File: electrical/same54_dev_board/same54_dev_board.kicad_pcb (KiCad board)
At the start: 2 copper layers, 177.8 x 83.8 mm, 0 parts

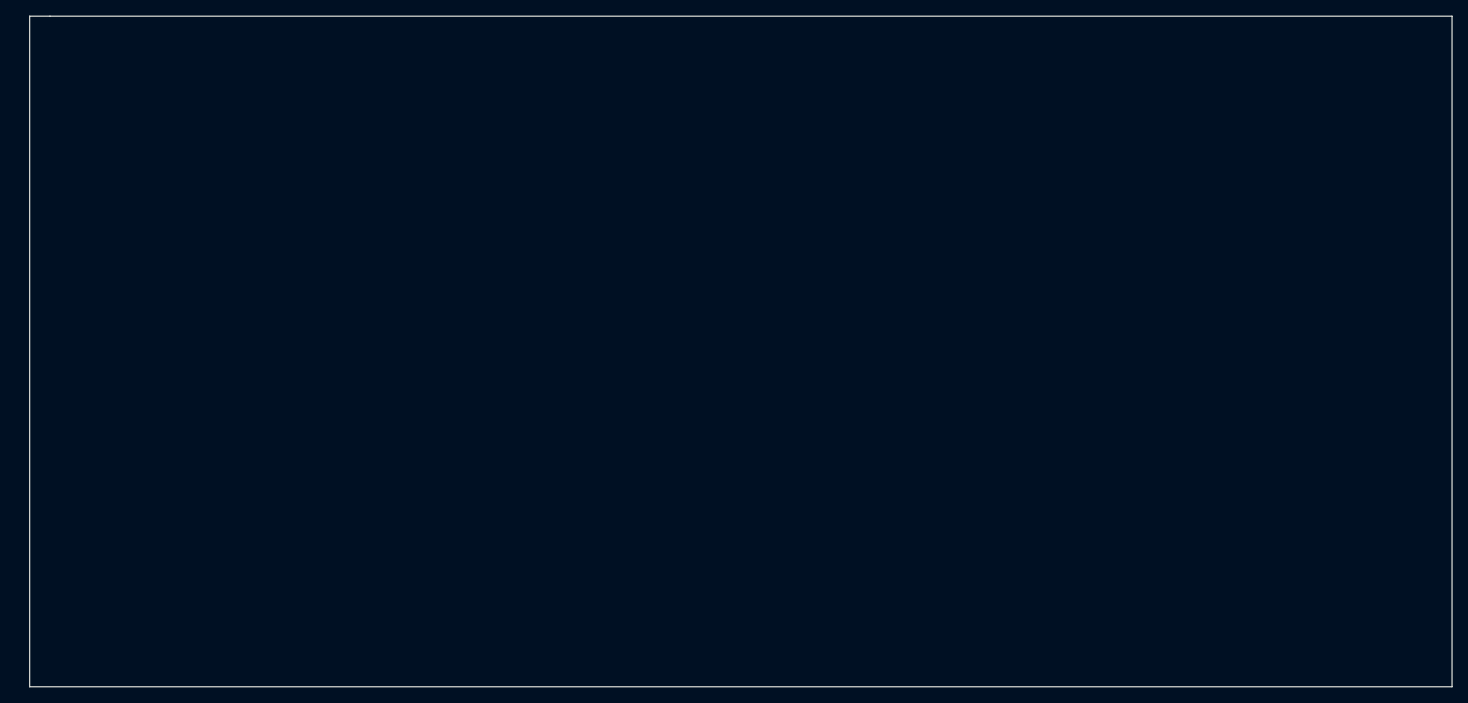
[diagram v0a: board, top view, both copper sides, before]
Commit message: Added hierarchical pins for some components, finished io expander to lcd bus, going with 2x20 icd block header for the tft bus but dont have a part number for digikey
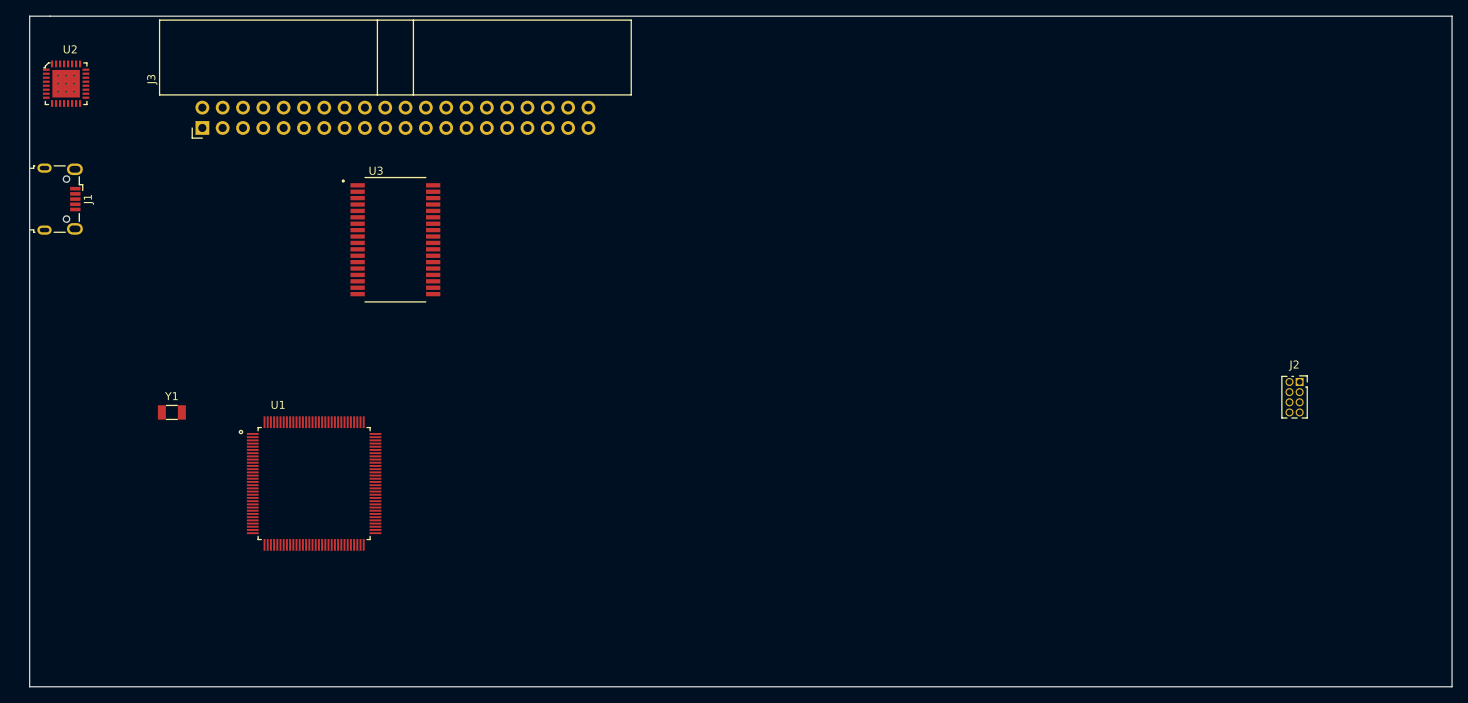
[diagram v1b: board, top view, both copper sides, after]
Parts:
- added J1: USB_B_Micro, Connector_USB:USB_Micro-B_Wuerth_629105150521, F.Cu at (54.6, 73.7)
- added J2: Conn_ARM_JTAG_SWD_10, Connector_PinSocket_1.27mm:PinSocket_2x04_P1.27mm_Vertical, F.Cu at (209.6, 96.5)
- added J3: Conn_02x20_Odd_Even_LCD_INTF, Connector_IDC:IDC-Header_2x20_P2.54mm_Horizontal, F.Cu at (72.4, 64.8)
- added U1: p_ATSAME54P20A-AU, penguin:QFP40P1600X1600X120-128N_ATSAME54P20A, F.Cu at (86.4, 109.2)
- added U2: FT232RQ-REEL, digikey-footprints:QFN-32-1EP_5x5mm, F.Cu at (55.9, 59.7)
- added U3: MAX7301AAX+, proj_modules:SOP80P1030X264-36N, F.Cu at (96.5, 78.7)
- added Y1: XOSC32, Crystal:Crystal_SMD_3215-2Pin_3.2x1.5mm, F.Cu at (68.6, 100.3)

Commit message: Trying to figure out how I want to do power...
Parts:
- J2: footprint Connector_PinSocket_1.27mm:PinSocket_2x04_P1.27mm_Vertical -> Connector_PinHeader_1.27mm:PinHeader_2x05_P1.27mm_Vertical
- moved U1 20.4 mm to (106.7, 110.5)
- turned U3 to 90 degrees
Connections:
- net /g_SCREEN_INTF/D0 renamed /s_SCREEN_INTF/D0
- net /g_SCREEN_INTF/D1 renamed /s_SCREEN_INTF/D1
- net /g_SCREEN_INTF/D10 renamed /s_SCREEN_INTF/D10
- net /g_SCREEN_INTF/D11 renamed /s_SCREEN_INTF/D11
- net /g_SCREEN_INTF/D12 renamed /s_SCREEN_INTF/D12
- net /g_SCREEN_INTF/D13 renamed /s_SCREEN_INTF/D13
- net /g_SCREEN_INTF/D14 renamed /s_SCREEN_INTF/D14
- net /g_SCREEN_INTF/D15 renamed /s_SCREEN_INTF/D15
- net /g_SCREEN_INTF/D16 renamed /s_SCREEN_INTF/D16
- net /g_SCREEN_INTF/D17 renamed /s_SCREEN_INTF/D17
- net /g_SCREEN_INTF/D18 renamed /s_SCREEN_INTF/D18
- net /g_SCREEN_INTF/D19 renamed /s_SCREEN_INTF/D19
- net /g_SCREEN_INTF/D2 renamed /s_SCREEN_INTF/D2
- net /g_SCREEN_INTF/D20 renamed /s_SCREEN_INTF/D20
- net /g_SCREEN_INTF/D21 renamed /s_SCREEN_INTF/D21
- net /g_SCREEN_INTF/D22 renamed /s_SCREEN_INTF/D22
- net /g_SCREEN_INTF/D23 renamed /s_SCREEN_INTF/D23
- net /g_SCREEN_INTF/D3 renamed /s_SCREEN_INTF/D3
- net /g_SCREEN_INTF/D4 renamed /s_SCREEN_INTF/D4
- net /g_SCREEN_INTF/D5 renamed /s_SCREEN_INTF/D5
- net /g_SCREEN_INTF/D6 renamed /s_SCREEN_INTF/D6
- net /g_SCREEN_INTF/D7 renamed /s_SCREEN_INTF/D7
- net /g_SCREEN_INTF/D8 renamed /s_SCREEN_INTF/D8
- net /g_SCREEN_INTF/D9 renamed /s_SCREEN_INTF/D9
- net /g_SCREEN_INTF/MASTER_SPI_CLK renamed /s_SCREEN_INTF/MASTER_SPI_CLK
- net /g_SCREEN_INTF/MASTER_SPI_MISO renamed /s_SCREEN_INTF/MASTER_SPI_MISO
- net /g_SCREEN_INTF/MASTER_SPI_MOSI renamed /s_SCREEN_INTF/MASTER_SPI_MOSI
- net /g_SCREEN_INTF/TFT_RSDC renamed /s_SCREEN_INTF/TFT_RSDC
- net /g_SCREEN_INTF/TFT_STB renamed /s_SCREEN_INTF/TFT_STB
- net /g_SCREEN_INTF/TFT_TE renamed /s_SCREEN_INTF/TFT_TE
- net /g_SCREEN_INTF/TFT_TOUCH_INT renamed /s_SCREEN_INTF/TFT_TOUCH_INT
- net /g_SCREEN_INTF/TFT_TOUCH_SCL renamed /s_SCREEN_INTF/TFT_TOUCH_SCL
- net /g_SCREEN_INTF/TFT_TOUCH_SDA renamed /s_SCREEN_INTF/TFT_TOUCH_SDA
- net /g_SCREEN_INTF/~IO_EXPANDER_CS renamed /s_SCREEN_INTF/~IO_EXPANDER_CS
- net /g_SCREEN_INTF/~TFT_CS renamed /s_SCREEN_INTF/~TFT_CS
- net /g_SCREEN_INTF/~TFT_RD renamed /s_SCREEN_INTF/~TFT_RD
- net /g_SCREEN_INTF/~TFT_RST renamed /s_SCREEN_INTF/~TFT_RST
- net /g_SCREEN_INTF/~TFT_WR renamed /s_SCREEN_INTF/~TFT_WR
- U1 pad 25: Net-(U1-Pad25) -> Net-(U1-Pad14)

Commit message: Added usart, i2c, and spi pin locations, as well as labeled sercoms
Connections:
- J1 pad 1: Net-(J1-Pad1) -> g_5v
- J1 pad 5: Net-(J1-Pad5) -> GND
- J1 pad 6: Net-(J1-Pad6) -> GND
- U2 pad 1: Net-(U2-Pad1) -> /s_USB_INTF.sch/3v3_Enable
- U2 pad 16: Net-(U2-Pad16) -> /s_USB_INTF.sch/3v3_Enable
- U2 pad 17: Net-(U2-Pad17) -> GND
- U2 pad 19: Net-(U2-Pad19) -> g_5v
- U2 pad 20: Net-(U2-Pad20) -> GND
- U2 pad 24: Net-(U2-Pad24) -> GND
- U2 pad 26: Net-(U2-Pad26) -> GND
- U2 pad 33: Net-(U2-Pad33) -> GND
- U2 pad 4: Net-(U2-Pad4) -> GND
- U2 pad 9: Net-(U2-Pad9) -> /s_USB_INTF.sch/3v3_Enable

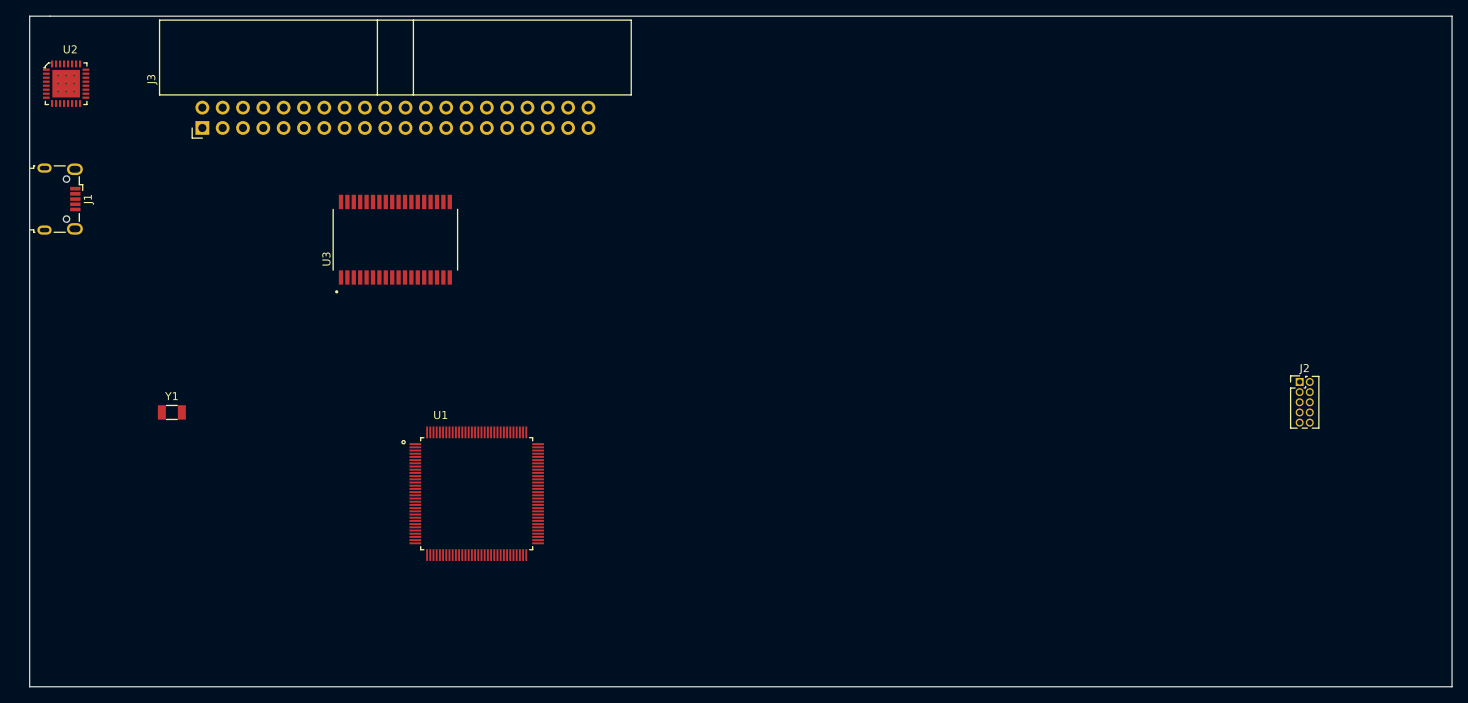
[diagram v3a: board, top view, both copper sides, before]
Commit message: Made board smaller, changed some small things
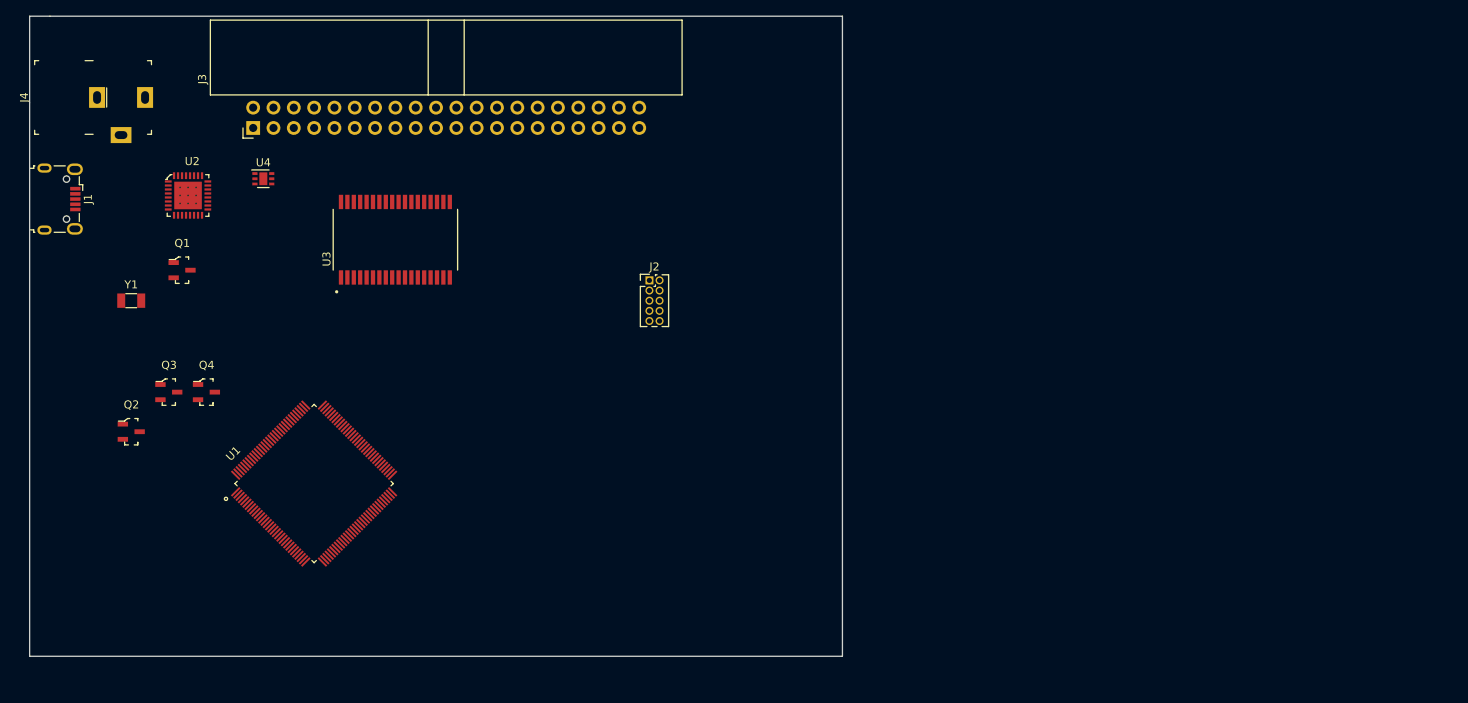
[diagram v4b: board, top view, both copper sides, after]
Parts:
- added J4: Barrel_Jack_Switch, digikey-footprints:Barrel_Jack_5.5mmODx2.1mmID_PJ-102A, F.Cu at (62.2, 61.0)
- added Q1: Default PFET_A, digikey-footprints:SOT-23-3, F.Cu at (69.8, 82.5)
- added Q2: Alt PFET_A, digikey-footprints:SOT-23-3, F.Cu at (63.5, 102.7)
- added Q3: Default PFET_B, digikey-footprints:SOT-23-3, F.Cu at (68.2, 97.8)
- added Q4: Alt PFET_B, digikey-footprints:SOT-23-3, F.Cu at (72.9, 97.8)
- added U4: NCP349MNAETBG, Package_DFN_QFN:DFN-6-1EP_2x2mm_P0.65mm_EP1x1.6mm, F.Cu at (80.0, 71.1)
- moved J2 82.3 mm to (128.3, 83.8)
- moved U2 20.7 mm to (71.1, 73.7)
- moved U1 20.4 mm to (86.4, 109.2), turned to 45 degrees
- moved Y1 14.9 mm to (63.5, 86.4)
- moved J3 6.35 mm to (78.7, 64.8)
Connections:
- net /s_SCREEN_INTF/MASTER_SPI_MOSI renamed /MASTER_SPI_MOSI
- net /s_SCREEN_INTF/~TFT_CS renamed /~TFT_CS
- net /s_USB_INTF.sch/3v3_Enable renamed /s_USB_INTF.sch/FTDI_3V3
- net Net-(J2-Pad10) renamed /s_BRAIN/~SYS_RST
- net Net-(J2-Pad2) renamed /s_BRAIN/SWDIO
- net Net-(J2-Pad4) renamed /s_BRAIN/SWCLK
- net Net-(J2-Pad6) renamed /s_BRAIN/SWO
- net Net-(U1-Pad11) renamed /s_BRAIN/EXT_IRQ_3
- net Net-(U1-Pad12) renamed /s_BRAIN/EXT_IRQ_4
- net Net-(U1-Pad125) renamed /s_BRAIN/EXT_IRQ_0
- net Net-(U1-Pad126) renamed /s_BRAIN/EXT_IRQ_1
- net Net-(U1-Pad127) renamed /s_BRAIN/EXT_IRQ_2
- net Net-(U1-Pad17) renamed /s_BRAIN/EXT_IRQ_5
- J1 pad 1: g_5v -> Net-(C7-Pad1)
- J2 pad 3: Net-(J2-Pad3) -> GND
- J2 pad 5: Net-(J2-Pad3) -> GND
- J2 pad 9: Net-(J2-Pad9) -> GND
- J3 pad 3: /s_SCREEN_INTF/TFT_TOUCH_SCL -> /MASTER_I2C_SCL
- J3 pad 4: /s_SCREEN_INTF/TFT_TOUCH_SDA -> /MASTER_I2C_SDA
- U1 pad 100: Net-(U1-Pad100) -> /DEBUG_RX
- U1 pad 101: Net-(U1-Pad101) -> /DEBUG_TX
- U1 pad 118: Net-(U1-Pad118) -> Net-(U1-Pad107)
- U1 pad 21: Net-(U1-Pad21) -> /MASTER_SPI_MISO
- U1 pad 22: Net-(U1-Pad22) -> /MASTER_SPI_CLK
- U1 pad 23: Net-(U1-Pad23) -> /MASTER_SPI_MISO
- U1 pad 46: Net-(U1-Pad46) -> Net-(U1-Pad107)
- U1 pad 54: Net-(U1-Pad54) -> Net-(U1-Pad107)
- U1 pad 65: Net-(U1-Pad65) -> Net-(U1-Pad107)
- U1 pad 66: Net-(U1-Pad66) -> /MASTER_I2C_SDA
- U1 pad 67: Net-(U1-Pad67) -> /MASTER_I2C_SCL
- U1 pad 79: Net-(U1-Pad79) -> Net-(U1-Pad107)
- U1 pad 91: Net-(U1-Pad91) -> Net-(U1-Pad107)
- U1 pad 97: Net-(U1-Pad97) -> Net-(U1-Pad107)
- U2 pad 19: g_5v -> /s_USB_INTF.sch/FTDI_5V
- U3 pad 33: /s_SCREEN_INTF/MASTER_SPI_CLK -> /MASTER_SPI_CLK
- U3 pad 4: /s_SCREEN_INTF/MASTER_SPI_MISO -> /MASTER_SPI_MISO
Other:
- board size 177.8 x 83.8 mm -> 101.6 x 80 mm
